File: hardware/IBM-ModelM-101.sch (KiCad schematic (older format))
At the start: 46 parts, among them J1 CONN-MOLEX-0670688000-USB-B, J2 KEYBOARD_ACTIVE_LINES, J3 KEYBOARD_INPUT_LINES, J4 CHASSIS_GROUND, J5 STATUS_LEDS, J6 DEBUG_FTDI, J7 JTAG, SW1 BOOT0, SW2 RESET, U1 TLV70233DBV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

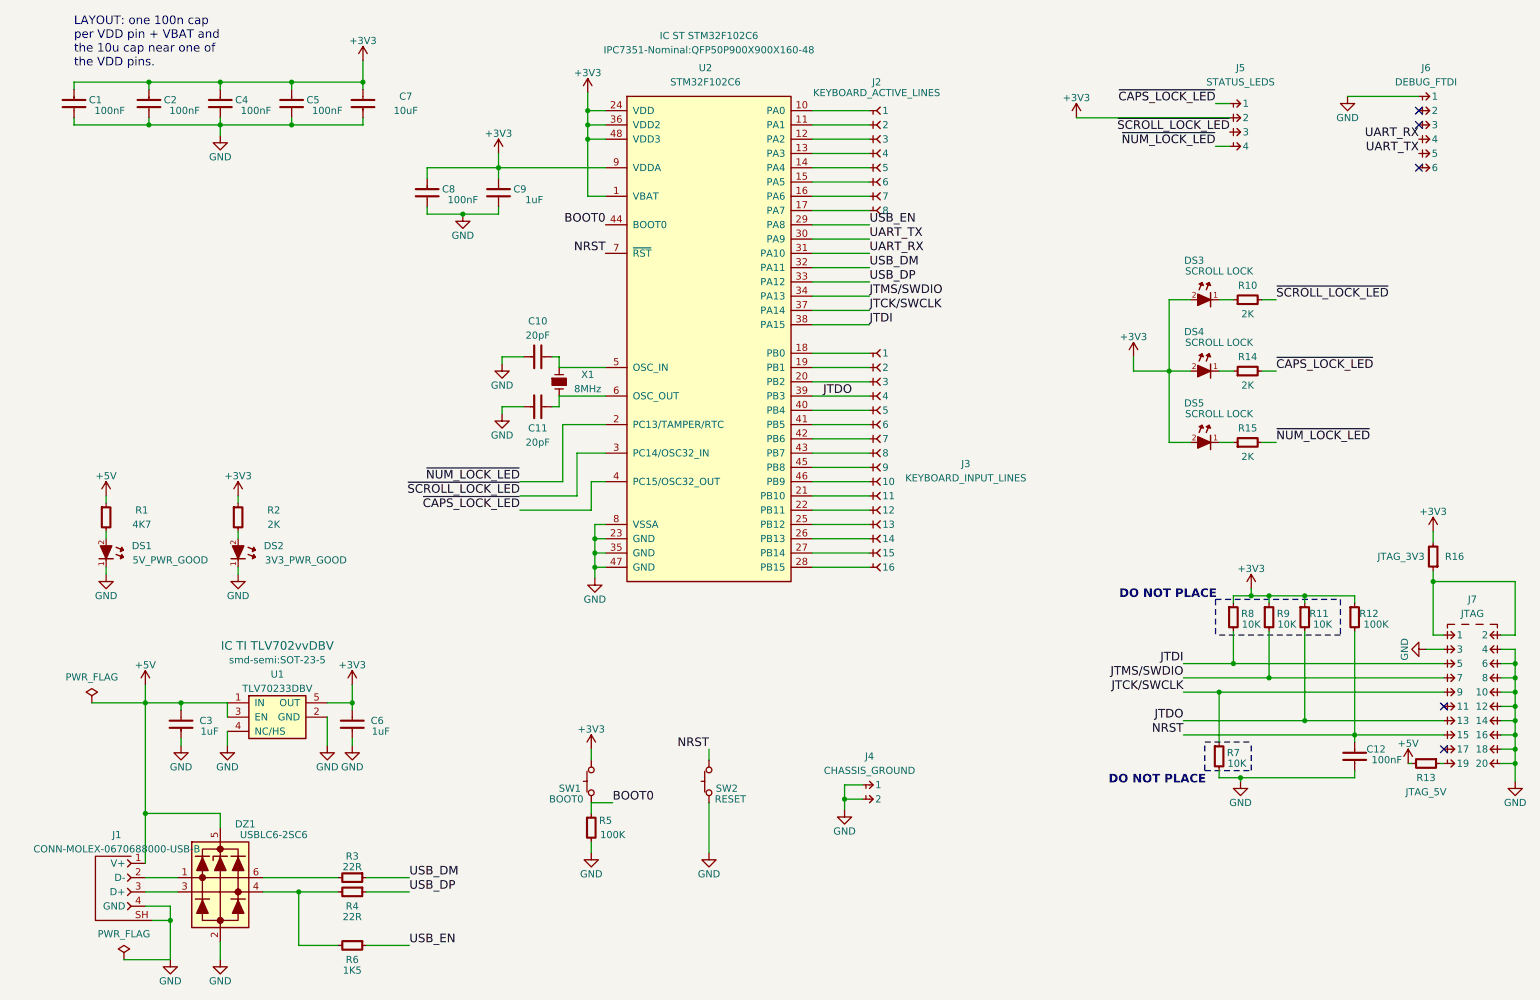
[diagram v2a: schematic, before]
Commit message: Updated schematic and PCB layout to fix errors in first revision.
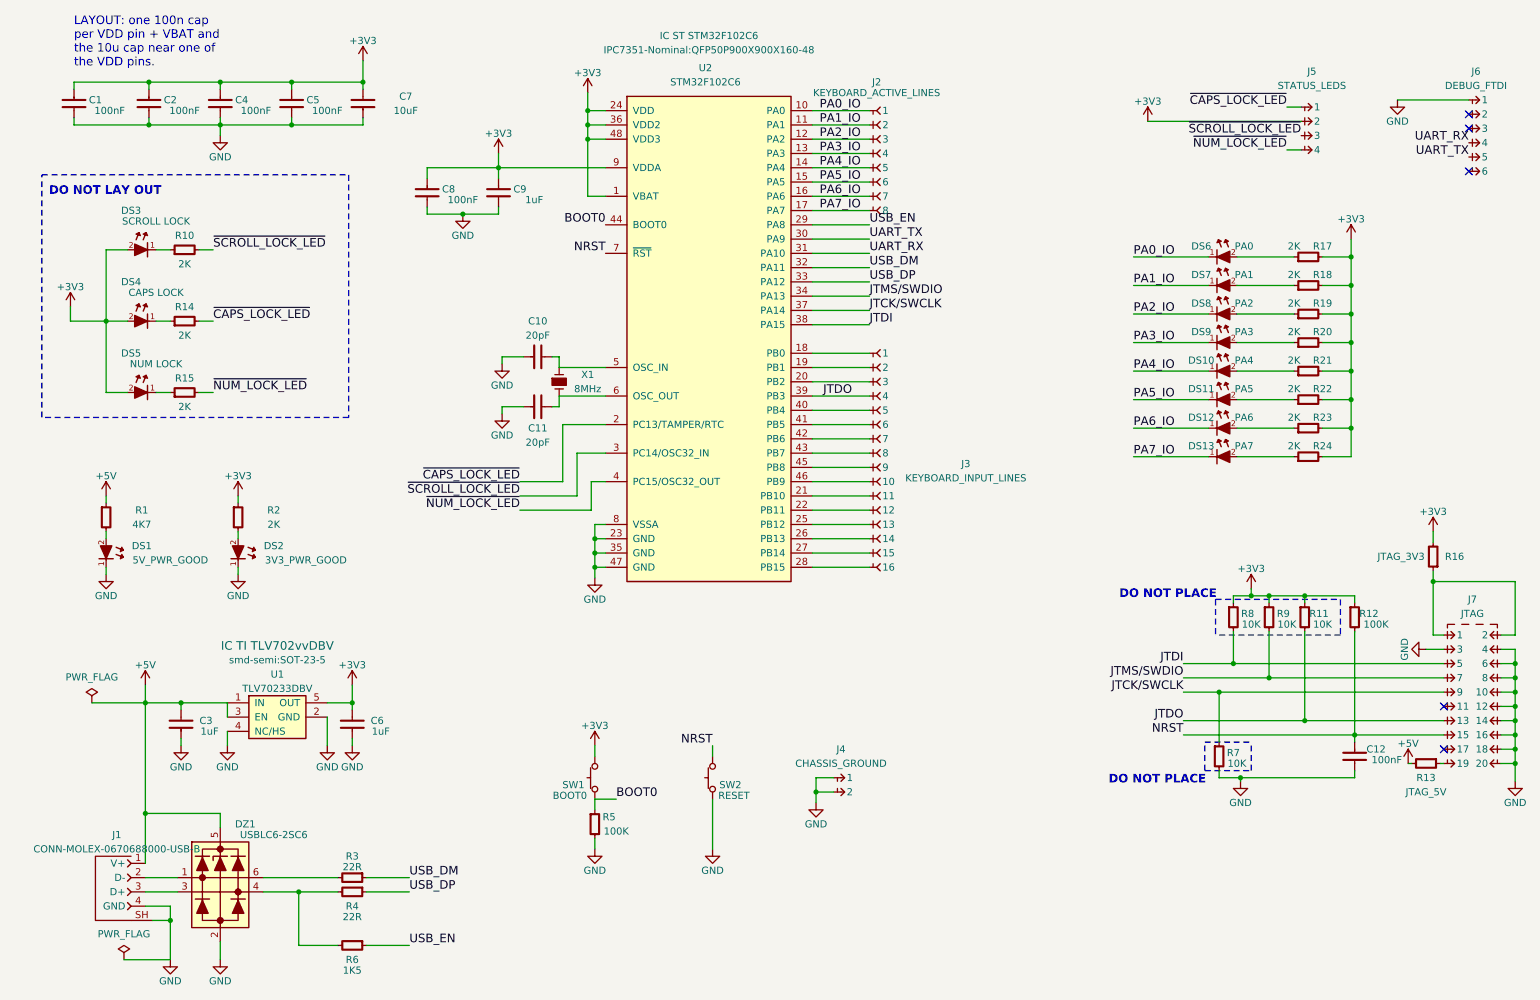
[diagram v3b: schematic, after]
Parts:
- added DS10: PA4, smd-semi:LED-0603, symbol LED-0603
- added DS11: PA5, smd-semi:LED-0603, symbol LED-0603
- added DS12: PA6, smd-semi:LED-0603, symbol LED-0603
- added DS13: PA7, smd-semi:LED-0603, symbol LED-0603
- added DS6: PA0, smd-semi:LED-0603, symbol LED-0603
- added DS7: PA1, smd-semi:LED-0603, symbol LED-0603
- added DS8: PA2, smd-semi:LED-0603, symbol LED-0603
- added DS9: PA3, smd-semi:LED-0603, symbol LED-0603
- added R17, R18, R19, R20, R21, R22, R23, R24: 2K, IPC7351-Nominal:RESC1608X50, symbol R-0603
- DS4: value SCROLL LOCK -> CAPS LOCK
- DS5: value SCROLL LOCK -> NUM LOCK
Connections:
- net +3V3: now also R17.2, R18.2, R19.2, R20.2, R21.2, R22.2, R23.2, R24.2
- net ~CAPS_LOCK_LED~: now also U2.2 (PC13/TAMPER/RTC); no longer U2.4 (PC15/OSC32_OUT)
- net ~NUM_LOCK_LED~: now also U2.4 (PC15/OSC32_OUT); no longer U2.2 (PC13/TAMPER/RTC)
- net PA0_IO: now reaches J2.1, U2.10 (PA0)
- net PA0_IO: now also DS6.1 (K)
- net PA1_IO: now reaches J2.2, U2.11 (PA1)
- net PA1_IO: now also DS7.1 (K)
- net PA2_IO: now reaches J2.3, U2.12 (PA2)
- net PA2_IO: now also DS8.1 (K)
- net PA3_IO: now reaches J2.4, U2.13 (PA3)
- net PA3_IO: now also DS9.1 (K)
- net PA4_IO: now reaches J2.5, U2.14 (PA4)
- net PA4_IO: now also DS10.1 (K)
- net PA5_IO: now reaches J2.6, U2.15 (PA5)
- net PA5_IO: now also DS11.1 (K)
- net PA6_IO: now reaches J2.7, U2.16 (PA6)
- net PA6_IO: now also DS12.1 (K)
- net PA7_IO: now reaches J2.8, U2.17 (PA7)
- net PA7_IO: now also DS13.1 (K)
- new net: DS6.2 (A), R17.1
- new net: DS7.2 (A), R18.1
- new net: DS8.2 (A), R19.1
- new net: DS9.2 (A), R20.1
- new net: DS10.2 (A), R21.1
- new net: DS11.2 (A), R22.1
- new net: DS12.2 (A), R23.1
- new net: DS13.2 (A), R24.1
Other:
- note added: "DO NOT LAY OUT"
- moved on the sheet: DS3, DS4, DS5, J4, J5, J6, R10, R14, R15, R5, SW1, SW2
